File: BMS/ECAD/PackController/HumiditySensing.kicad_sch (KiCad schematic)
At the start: 0 parts

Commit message: pack controller close to finished and startet pack controller
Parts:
- added C18, C5: 1nF 0603 16V, Capacitor_SMD:C_0603_1608Metric_Pad1.08x0.95mm_HandSolder, symbol Device:C
- added R10, R14, R30, R31: 10kR 0603, Resistor_SMD:R_0603_1608Metric_Pad0.98x0.95mm_HandSolder, symbol Device:R
- added R11, R15: 1MR 0603, Resistor_SMD:R_0603_1608Metric_Pad0.98x0.95mm_HandSolder, symbol Device:R
- added R12, R16: R_Leak, Resistor_SMD:R_0603_1608Metric_Pad0.98x0.95mm_HandSolder, symbol Device:R
- added R13, R17: 10MR 0603, Resistor_SMD:R_0603_1608Metric_Pad0.98x0.95mm_HandSolder, symbol Device:R
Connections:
- new net GND: C18.1, C5.1, R11.2, R15.2
- new net R_Leak1_ElecIn: R10.2, R12.1, R13.1
- new net R_Leak1_ElecOut: R11.1, R12.2, R13.2, R30.2
- new net R_Leak1_Signal: C5.2, R30.1
- new net R_Leak1_Supply: R10.1
- new net R_Leak2_ElecIn: R14.2, R16.1, R17.1
- new net R_Leak2_ElecOut: R15.1, R16.2, R17.2, R31.2
- new net R_Leak2_Signal: C18.2, R31.1
- new net R_Leak2_Supply: R14.1
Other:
- note added: "Leakage sensor: Flex electrodes form R_LEAK. R_EOL = 10M is mounted on the flex sensor, parallel to the electrodes, for open-wire detection. R_SENSOR = R_LEAK || R_EOL Measurement: Pulse R_Leak_Supply HIGH, wait 10...50ms, sample ADC, then set supply LOW/Hi-Z. Suggested scan rate: 1Hz. ADC conversion, assuming ADC reference = VDD and R_Leak_Supply = VDD: x = ADC_raw / ADC_max R_SENSOR = R_REF * (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"

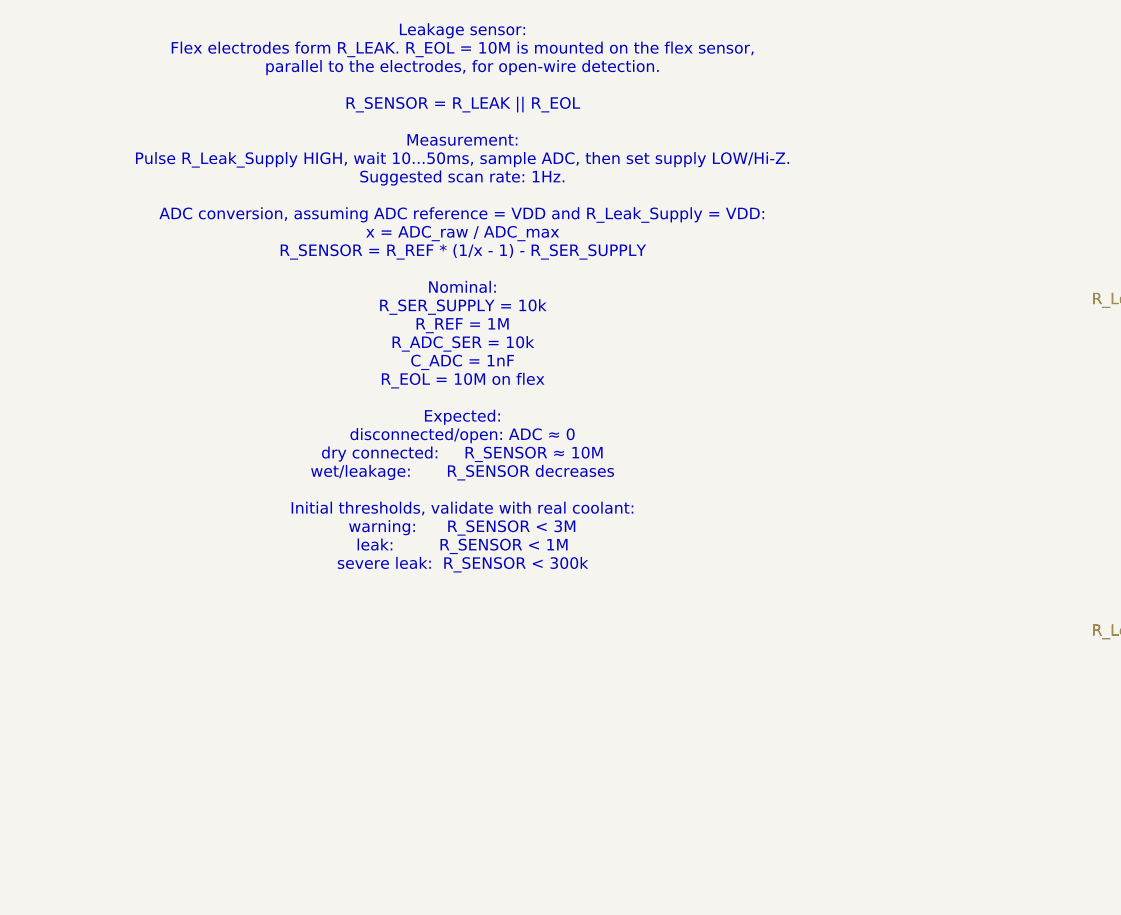
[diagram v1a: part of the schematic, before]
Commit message: finished schemativ of precharge
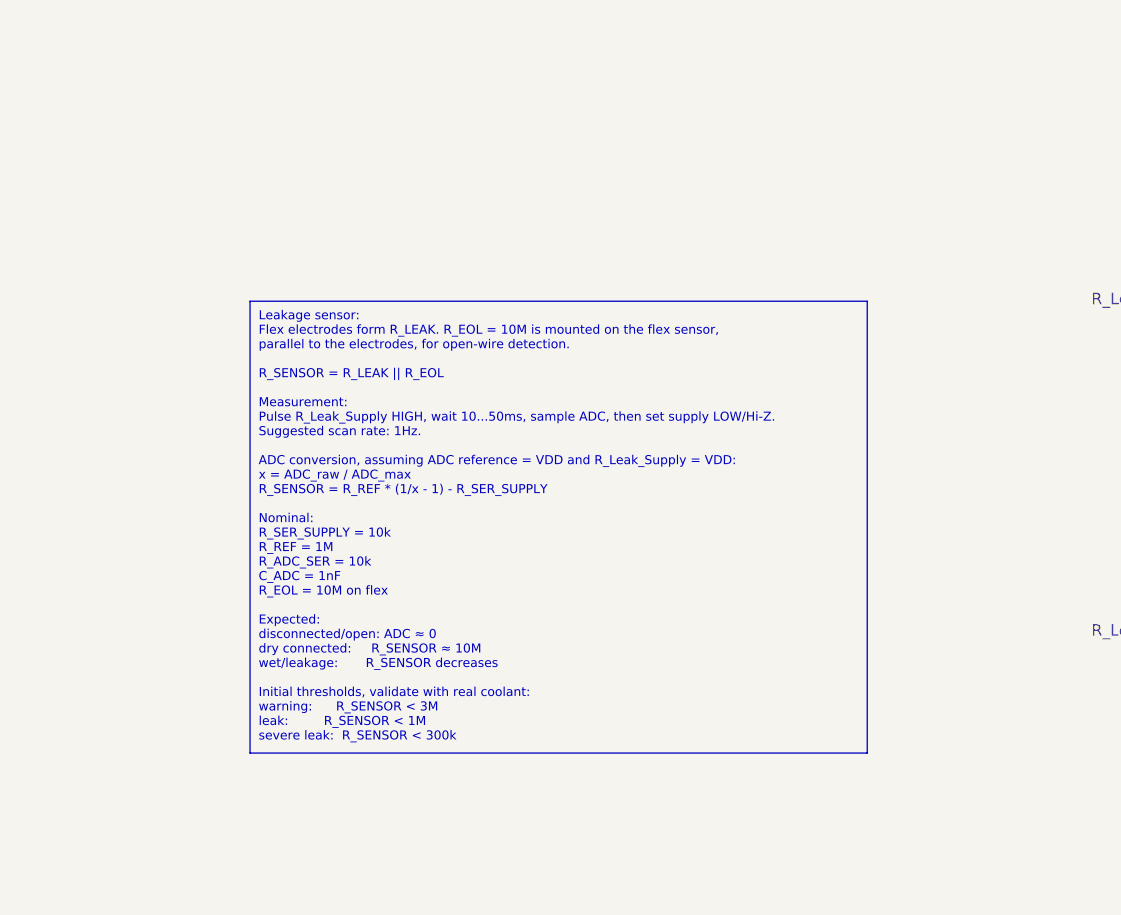
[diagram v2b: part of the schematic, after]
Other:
- note removed: "Leakage sensor: Flex electrodes form R_LEAK. R_EOL = 10M is mounted on the flex sensor, parallel to the electrodes, for open-wire detection. R_SENSOR = R_LEAK || R_EOL Measurement: Pulse R_Leak_Supply HIGH, wait 10...50ms, sample ADC, then set supply LOW/Hi-Z. Suggested scan rate: 1Hz. ADC conversion, assuming ADC reference = VDD and R_Leak_Supply = VDD: x = ADC_raw / ADC_max R_SENSOR = R_REF * (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"
- title: (none) -> PackController
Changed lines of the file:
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@@
 	(paper "A4")
 	(title_block
+		(title "PackController")
 		(date "2026-03-03")
 		(rev "V0.9")
@@
 		)
 	)
-	(text "Leakage sensor:\nFlex electrodes form R_LEAK. R_EOL = 10M is mounted on the flex sensor,\nparallel to the electrodes, for open-wire detection.\n\nR_SENSOR = R_LEAK || R_EOL\n\nMeasurement:\nPulse R_Leak_Supply HIGH, wait 10...50ms, sample ADC, then set supply LOW/Hi-Z.\nSuggested scan rate: 1Hz.\n\nADC conversion, assuming ADC reference = VDD and R_Leak_Supply = VDD:\nx = ADC_raw / ADC_max\nR_SENSOR = R_REF * (1/x - 1) - R_SER_SUPPLY\n\nNominal:\nR_SER_SUPPLY = 10k\nR_REF = 1M\nR_ADC_SER = 10k\nC_ADC = 1nF\nR_EOL = 10M on flex\n\nExpected:\ndisconnected/open: ADC ≈ 0\ndry connected:     R_SENSOR ≈ 10M\nwet/leakage:       R_SENSOR decreases\n\nInitial thresholds, validate with real coolant:\nwarning:      R_SENSOR < 3M\nleak:         R_SENSOR < 1M\nsevere leak:  R_SENSOR < 300k"
+	(text_box "Leakage sensor:\nFlex electrodes form R_LEAK. R_EOL = 10M is mounted on the flex sensor,\nparallel to the electrodes, for open-wire detection.\n\nR_SENSOR = R_LEAK || R_EOL\n\nMeasurement:\nPulse R_Leak_Supply HIGH, wait 10...50ms, sample ADC, then set supply LOW/Hi-Z.\nSuggested scan rate: 1Hz.\n\nADC conversion, assuming ADC reference = VDD and R_Leak_Supply = VDD:\nx = ADC_raw / ADC_max\nR_SENSOR = R_REF * (1/x - 1) - R_SER_SUPPLY\n\nNominal:\nR_SER_SUPPLY = 10k\nR_REF = 1M\nR_ADC_SER = 10k\nC_ADC = 1nF\nR_EOL = 10M on flex\n\nExpected:\ndisconnected/open: ADC ≈ 0\ndry connected:     R_SENSOR ≈ 10M\nwet/leakage:       R_SENSOR decreases\n\nInitial thresholds, validate with real coolant:\nwarning:      R_SENSOR < 3M\nleak:         R_SENSOR < 1M\nsevere leak:  R_SENSOR < 300k"
 		(exclude_from_sim no)
-		(at 60.452 50.8 0)
+		(at 36.83 51.0579 0)
+		(size 68.58 50.2022)
+		(margins 0.9525 0.9525 0.9525 0.9525)
+		(stroke
+			(width 0)
+			(type solid)
+			(color 0 0 0 1)
+		)
+		(fill
+			(type color)
+			(color 255 255 194 1)
+		)
 		(effects
 			(font
-				(size 1.27 1.27)
+				(size 1 1)
+				(color 0 0 0 1)
 			)
+			(justify left top)
 		)
 	)
